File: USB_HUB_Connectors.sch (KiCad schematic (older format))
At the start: 86 parts, among them IC4 AP22652W6-7, J10 E8124-015-01, J11 E8124-015-01, U15 USB57442G, Y2 ABM8G-25.000MHZ-B4Y-T

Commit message: Connected differential signals from camera modules and LCD display. Without checking track lengths
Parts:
- C160: footprint antmicro-footprints:0402-cap -> sc606-baseboard-footprints:0402-cap; symbol antmicroCapacitors0402:C_10u_0402 -> sc606-baseboard:C_10u_0402
- C161: footprint antmicro-footprints:0805-cap -> sc606-baseboard-footprints:0805-cap; symbol antmicroCapacitorsmisc:C_100u_0805 -> sc606-baseboard:C_100u_0805
- FB2: footprint antmicro-footprints:0603 -> sc606-baseboard-footprints:0603; symbol antmicroFerriteBeadsandChips:BLM18EG221SN1D -> sc606-baseboard:BLM18EG221SN1D
- IC4: footprint antmicro-footprints:SOT-23-6 -> sc606-baseboard-footprints:SOT-23-6; symbol antmicroPMICPowerDistributionSwitchesLoadDrivers:AP22652W6-7 -> sc606-baseboard:AP22652W6-7
- R171: footprint antmicro-footprints:0402-res -> sc606-baseboard-footprints:0402-res; symbol antmicroResistors0402:R_10k_0402 -> sc606-baseboard:R_10k_0402
- R172: footprint antmicro-footprints:0402-res -> sc606-baseboard-footprints:0402-res; symbol antmicroResistors0402:R_470R_0402 -> sc606-baseboard:R_470R_0402
- R173: footprint antmicro-footprints:0402-res -> sc606-baseboard-footprints:0402-res; symbol antmicroResistors0402:R_12k4_0402 -> sc606-baseboard:R_12k4_0402
- R174: footprint antmicro-footprints:0402-res -> sc606-baseboard-footprints:0402-res; symbol antmicroResistors0402:R_0R_0402 -> sc606-baseboard:R_0R_0402
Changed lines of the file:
@@
 5V0_USB
 $Comp
-L antmicroResistors0402:R_0R_0402 R174
+L sc606-baseboard:R_0R_0402 R174
 U 1 1 621E9B7B
 P 14775 1150
 F 0 "R174" H 14775 1455 60  0000 C CNN
 F 1 "R_0R_0402" H 14775 1000 60  0001 C CNN
-F 2 "antmicro-footprints:0402-res" H 14975 1350 60  0001 L CNN
+F 2 "sc606-baseboard-footprints:0402-res" H 14975 1350 60  0001 L CNN
 F 3 "" H 14775 1150 50  0001 C CNN
 F 4 "PANASONIC" H 14975 1550 60  0001 L CNN "Manufacturer"
@@
 USB Load Switch
 $Comp
-L antmicroPMICPowerDistributionSwitchesLoadDrivers:AP22652W6-7 IC4
+L sc606-baseboard:AP22652W6-7 IC4
 U 1 1 622A09A8
 P 12975 2025
 F 0 "IC4" H 12975 2390 50  0000 C CNN
 F 1 "AP22652W6-7" H 12975 2299 50  0000 C CNN
-F 2 "antmicro-footprints:SOT-23-6" H 12975 1775 50  0001 C CNN
+F 2 "sc606-baseboard-footprints:SOT-23-6" H 12975 1775 50  0001 C CNN
 F 3 "https://www.diodes.com/assets/Datasheets/AP22652_53_52A_53A.pdf" H 12975 2025 50  0001 C CNN
 F 4 "Diodes Incorporated " H 12975 1675 50  0001 C CNN "Manufacturer"
@@
 $EndComp
 $Comp
-L antmicroResistors0402:R_12k4_0402 R173
+L sc606-baseboard:R_12k4_0402 R173
 U 1 1 622A18CE
 P 13550 2275
 F 0 "R173" V 13505 2345 60  0000 L CNN
 F 1 "R_12k4_0402" H 13550 2125 60  0001 C CNN
-F 2 "antmicro-footprints:0402-res" H 13750 2475 60  0001 L CNN
+F 2 "sc606-baseboard-footprints:0402-res" H 13750 2475 60  0001 L CNN
 F 3 "" H 13550 2275 50  0001 C CNN
 F 4 "PANASONIC_ELECTRONIC_COMPONENTS" H 13750 2675 60  0001 L CNN "Manufacturer"
@@
 $EndComp
 $Comp
-L sa800u-baseboard-hw:GND #PWR0197
+L sc606-baseboard:GND #PWR0197
 U 1 1 622A2939
 P 13550 2425
@@
 $EndComp
 $Comp
-L sa800u-baseboard-hw:GND #PWR0196
+L sc606-baseboard:GND #PWR0196
 U 1 1 622A2C10
 P 12575 2250
@@
 	13375 2125 13550 2125
 $Comp
-L antmicroCapacitors0402:C_10u_0402 C160
+L sc606-baseboard:C_10u_0402 C160
 U 1 1 622C6F25
 P 12075 2350
 F 0 "C160" H 12190 2395 60  0000 L CNN
 F 1 "C_10u_0402" H 12075 2200 60  0001 C CNN
-F 2 "antmicro-footprints:0402-cap" H 12275 2550 60  0001 L CNN
+F 2 "sc606-baseboard-footprints:0402-cap" H 12275 2550 60  0001 L CNN
 F 3 "" H 12075 2350 50  0001 C CNN
 F 4 "YAGEO" H 12275 2750 60  0001 L CNN "Manufacturer"
@@
 $EndComp
 $Comp
-L antmicroCapacitorsmisc:C_100u_0805 C161
+L sc606-baseboard:C_100u_0805 C161
 U 1 1 622C85ED
 P 14150 2200
 F 0 "C161" H 14265 2245 60  0000 L CNN
 F 1 "C_100u_0805" H 14150 2050 60  0001 C CNN
-F 2 "antmicro-footprints:0805-cap" H 14350 2400 60  0001 L CNN
+F 2 "sc606-baseboard-footprints:0805-cap" H 14350 2400 60  0001 L CNN
 F 3 "" H 14150 2200 50  0001 C CNN
 F 4 "MURATA" H 14350 2600 60  0001 L CNN "Manufacturer"
@@
 $EndComp
 $Comp
-L antmicroFerriteBeadsandChips:BLM18EG221SN1D FB2
+L sc606-baseboard:BLM18EG221SN1D FB2
 U 1 1 622CA454
 P 14375 1925
 F 0 "FB2" H 14375 2212 60  0000 C CNN
 F 1 "BLM18EG221SN1D" H 14375 2106 60  0000 C CNN
-F 2 "antmicro-footprints:0603" H 14575 2125 60  0001 L CNN
+F 2 "sc606-baseboard-footprints:0603" H 14575 2125 60  0001 L CNN
 F 3 "" H 14575 2225 60  0001 L CNN
 F 4 "BLM18EG221SN1D" H 14575 2425 60  0001 L CNN "MPN"
@@
 	14150 1925 14175 1925
 $Comp
-L sa800u-baseboard-hw:GND #PWR0198
+L sc606-baseboard:GND #PWR0198
 U 1 1 62349595
 P 14150 2350
@@
 $EndComp
 $Comp
-L sa800u-baseboard-hw:GND #PWR0195
+L sc606-baseboard:GND #PWR0195
 U 1 1 62349AB5
 P 12075 2500
@@
 $EndComp
 $Comp
-L antmicroResistors0402:R_10k_0402 R171
+L sc606-baseboard:R_10k_0402 R171
 U 1 1 62372BC6
 P 11725 1800
 F 0 "R171" V 11680 1870 60  0000 L CNN
 F 1 "R_10k_0402" H 11725 1650 60  0001 C CNN
-F 2 "antmicro-footprints:0402-res" H 11925 2000 60  0001 L CNN
+F 2 "sc606-baseboard-footprints:0402-res" H 11925 2000 60  0001 L CNN
 F 3 "" H 11725 1800 50  0001 C CNN
 F 4 "VISHAY" H 11925 2200 60  0001 L CNN "Manufacturer"
@@
 	11725 2025 12575 2025
 $Comp
-L antmicroResistors0402:R_470R_0402 R172
+L sc606-baseboard:R_470R_0402 R172
 U 1 1 62398B3D
 P 12300 1650
 F 0 "R172" H 12300 1863 60  0000 C CNN
 F 1 "R_470R_0402" H 12300 1500 60  0001 C CNN
-F 2 "antmicro-footprints:0402-res" H 12500 1850 60  0001 L CNN
+F 2 "sc606-baseboard-footprints:0402-res" H 12500 1850 60  0001 L CNN
 F 3 "" H 12300 1650 50  0001 C CNN
 F 4 "VISHAY" H 12500 2050 60  0001 L CNN "Manufacturer"

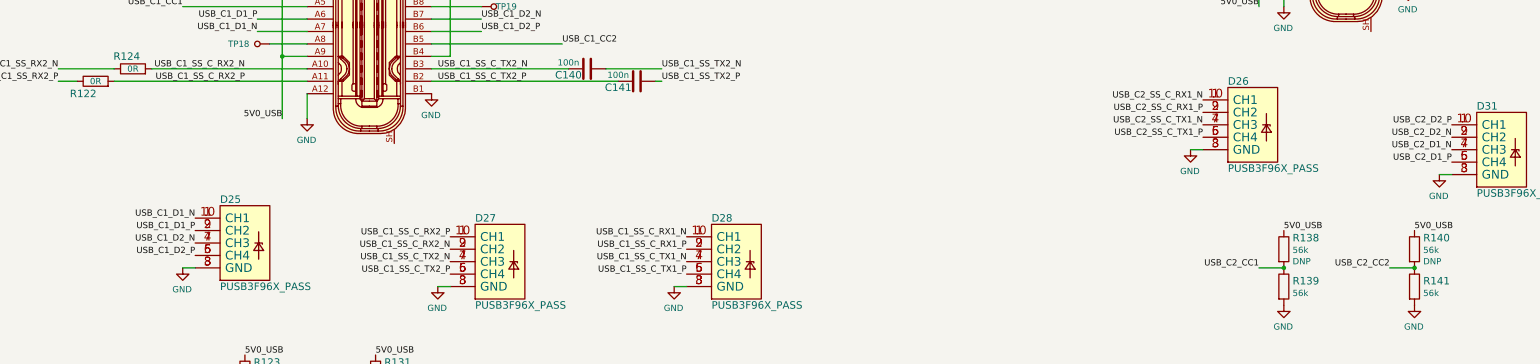
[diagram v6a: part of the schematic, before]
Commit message: Routed USB flash and both USB connectors differential signals with tuning
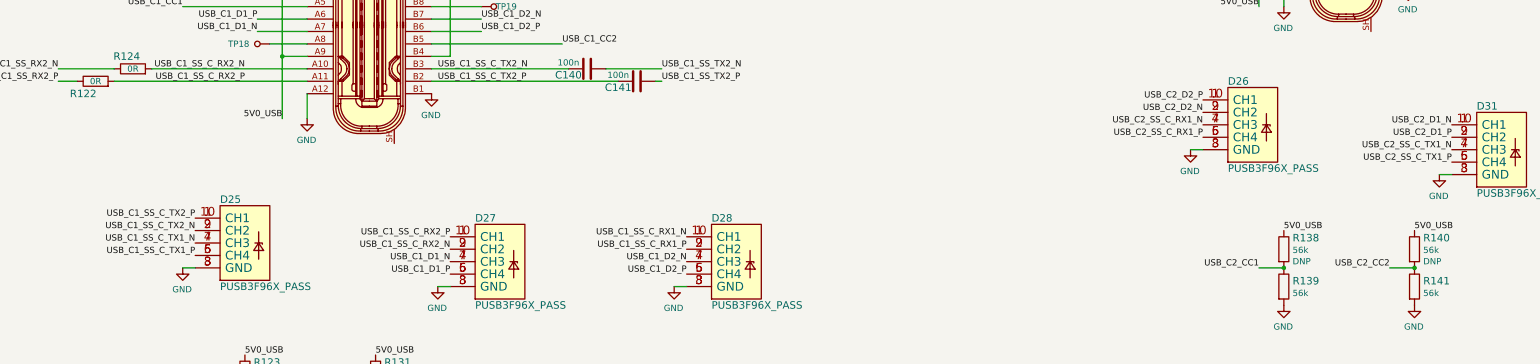
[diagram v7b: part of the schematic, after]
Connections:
- net USB_C1_D1_N: now also D27.4 (CH3), D27.7 (CH3); no longer D25.1 (CH1), D25.10 (CH1)
- net USB_C1_D1_P: now also D27.5 (CH4), D27.6 (CH4); no longer D25.2 (CH2), D25.9 (CH2)
- net USB_C1_D2_N: now also D28.4 (CH3), D28.7 (CH3); no longer D25.4 (CH3), D25.7 (CH3)
- net USB_C1_D2_P: now also D28.5 (CH4), D28.6 (CH4); no longer D25.5 (CH4), D25.6 (CH4)
- net USB_C1_SS_C_TX1_N: now also D25.4 (CH3), D25.7 (CH3); no longer D28.4 (CH3), D28.7 (CH3)
- net USB_C1_SS_C_TX1_P: now also D25.5 (CH4), D25.6 (CH4); no longer D28.5 (CH4), D28.6 (CH4)
- net USB_C1_SS_C_TX2_N: now also D25.2 (CH2), D25.9 (CH2); no longer D27.4 (CH3), D27.7 (CH3)
- net USB_C1_SS_C_TX2_P: now also D25.1 (CH1), D25.10 (CH1); no longer D27.5 (CH4), D27.6 (CH4)
- net USB_C2_D1_N: now also D31.1 (CH1), D31.10 (CH1); no longer D31.4 (CH3), D31.7 (CH3)
- net USB_C2_D1_P: now also D31.2 (CH2), D31.9 (CH2); no longer D31.5 (CH4), D31.6 (CH4)
- net USB_C2_D2_N: now also D26.2 (CH2), D26.9 (CH2); no longer D31.2 (CH2), D31.9 (CH2)
- net USB_C2_D2_P: now also D26.1 (CH1), D26.10 (CH1); no longer D31.1 (CH1), D31.10 (CH1)
- net USB_C2_SS_C_RX1_N: now also D26.4 (CH3), D26.7 (CH3); no longer D26.1 (CH1), D26.10 (CH1)
- net USB_C2_SS_C_RX1_P: now also D26.5 (CH4), D26.6 (CH4); no longer D26.2 (CH2), D26.9 (CH2)
- net USB_C2_SS_C_TX1_N: now also D31.4 (CH3), D31.7 (CH3); no longer D26.4 (CH3), D26.7 (CH3)
- net USB_C2_SS_C_TX1_P: now also D31.5 (CH4), D31.6 (CH4); no longer D26.5 (CH4), D26.6 (CH4)
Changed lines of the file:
@@
 	1    0    0    -1
 $EndComp
-Text Label 5000 9350 2    50   ~ 0
+Text Label 2950 8900 2    50   ~ 0
 USB_C1_SS_C_TX2_P
-Text Label 5000 9250 2    50   ~ 0
+Text Label 2950 9000 2    50   ~ 0
 USB_C1_SS_C_TX2_N
 $Comp
@@
 Wire Wire Line
 	6900 9450 6800 9450
-Text Label 2950 9000 2    50   ~ 0
+Text Label 5000 9350 2    50   ~ 0
 USB_C1_D1_P
-Text Label 2950 8900 2    50   ~ 0
+Text Label 5000 9250 2    50   ~ 0
 USB_C1_D1_N
 Wire Wire Line
@@
 Wire Wire Line
 	14900 8550 14800 8550
-Text Label 13050 8450 2    50   ~ 0
+Text Label 13050 8250 2    50   ~ 0
 USB_C2_D1_P
-Text Label 13050 8350 2    50   ~ 0
+Text Label 13050 8150 2    50   ~ 0
 USB_C2_D1_N
-Text Label 11050 7950 2    50   ~ 0
+Text Label 11050 8150 2    50   ~ 0
 USB_C2_SS_C_RX1_N
-Text Label 11050 8050 2    50   ~ 0
+Text Label 11050 8250 2    50   ~ 0
 USB_C2_SS_C_RX1_P
 Wire Wire Line
@@
 Wire Wire Line
 	3850 6550 3850 6800
-Text Label 6900 9350 2    50   ~ 0
+Text Label 2950 9200 2    50   ~ 0
 USB_C1_SS_C_TX1_P
-Text Label 6900 9250 2    50   ~ 0
+Text Label 2950 9100 2    50   ~ 0
 USB_C1_SS_C_TX1_N
 Text Label 5000 9150 2    50   ~ 0
@@
 	1    0    0    -1
 $EndComp
-Text Label 11050 8250 2    50   ~ 0
+Text Label 13050 8450 2    50   ~ 0
 USB_C2_SS_C_TX1_P
-Text Label 11050 8150 2    50   ~ 0
+Text Label 13050 8350 2    50   ~ 0
 USB_C2_SS_C_TX1_N
 $Comp
@@
 Wire Wire Line
 	7850 1200 8500 1200
-Text Label 13050 8150 2    50   ~ 0
+Text Label 11050 7950 2    50   ~ 0
 USB_C2_D2_P
-Text Label 13050 8250 2    50   ~ 0
+Text Label 11050 8050 2    50   ~ 0
 USB_C2_D2_N
-Text Label 2950 9200 2    50   ~ 0
+Text Label 6900 9350 2    50   ~ 0
 USB_C1_D2_P
-Text Label 2950 9100 2    50   ~ 0
+Text Label 6900 9250 2    50   ~ 0
 USB_C1_D2_N
 Wire Wire Line

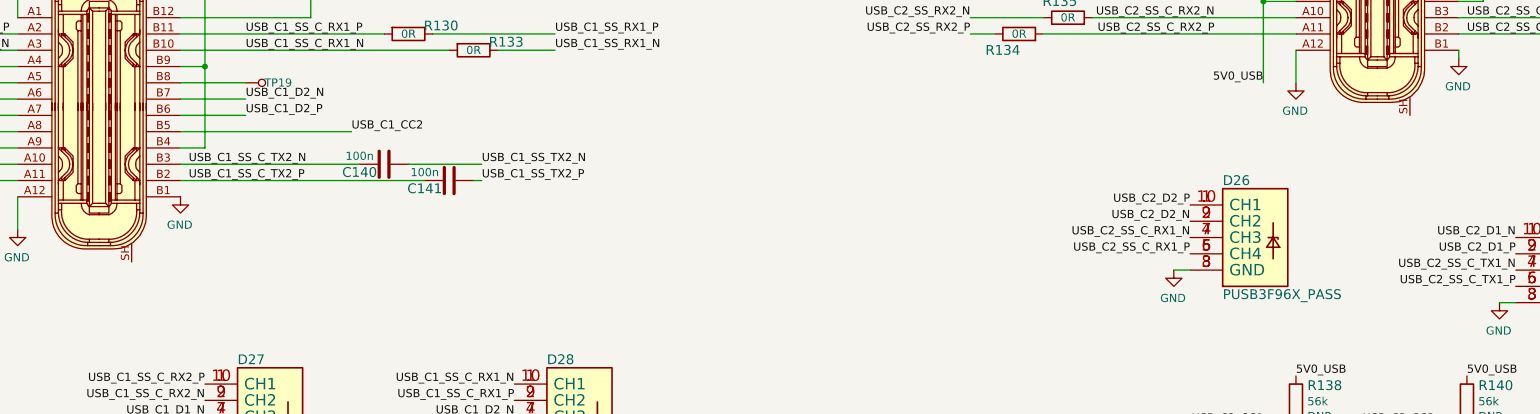
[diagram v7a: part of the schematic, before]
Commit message: Connected all signals for USB Flash and USB-C connectors
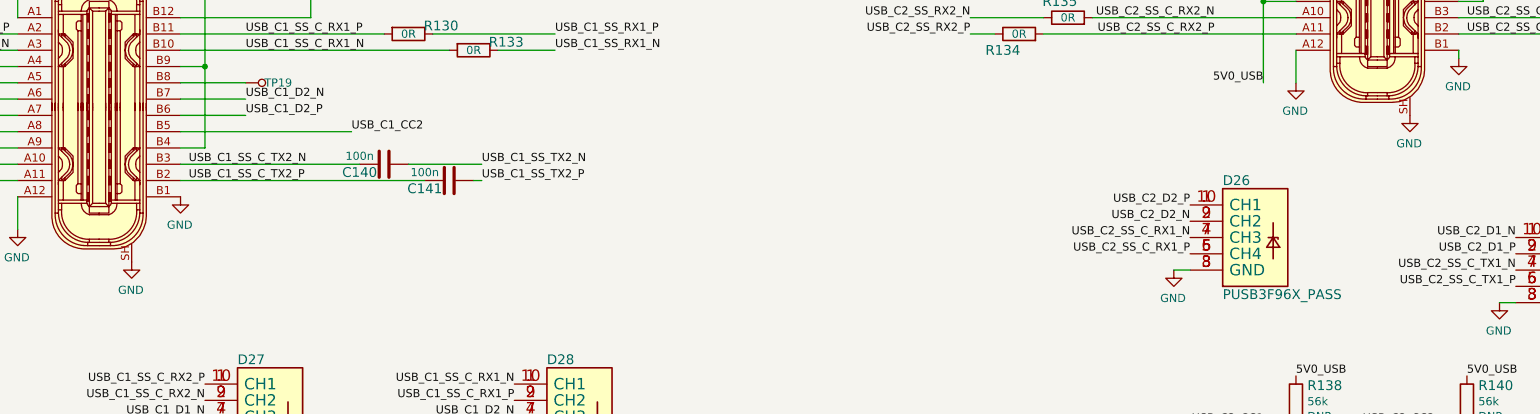
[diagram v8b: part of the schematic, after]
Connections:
- net GND: now also J10.SH, J11.SH
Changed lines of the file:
@@
 Wire Wire Line
 	5000 5950 5000 6350
+$Comp
+L sc606-baseboard:GND #PWR?
+U 1 1 620C24E5
+P 12400 7400
+AR Path="/61F60810/620C24E5" Ref="#PWR?"  Part="1"
+AR Path="/63348E64/620C24E5" Ref="#PWR?"  Part="1"
+F 0 "#PWR?" H 12400 7150 50  0001 C CNN
+F 1 "GND" H 12405 7227 50  0000 C CNN
+F 2 "" H 12400 7400 50  0001 C CNN
+F 3 "" H 12400 7400 50  0001 C CNN
+	1    12400 7400
+	-1   0    0    -1
+$EndComp
+$Comp
+L sc606-baseboard:GND #PWR?
+U 1 1 620CB62E
+P 4550 8300
+AR Path="/61F60810/620CB62E" Ref="#PWR?"  Part="1"
+AR Path="/63348E64/620CB62E" Ref="#PWR?"  Part="1"
+F 0 "#PWR?" H 4550 8050 50  0001 C CNN
+F 1 "GND" H 4555 8127 50  0000 C CNN
+F 2 "" H 4550 8300 50  0001 C CNN
+F 3 "" H 4550 8300 50  0001 C CNN
+	1    4550 8300
+	-1   0    0    -1
+$EndComp
 $EndSCHEMATC
